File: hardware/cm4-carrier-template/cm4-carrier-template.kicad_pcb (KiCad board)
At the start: 4 copper layers, 90 x 40 mm, 41 parts, among them J1 USB_C_Receptacle_USB2.0, J2 Micro_SD_Card, J3 Abracon_ARJM11-502, Q1 DMP2066LSN, SW1 BOOT, SW2 GLOBAL_EN, U5 Compute_Module_4_Functional, U6 TPD2EUSB30

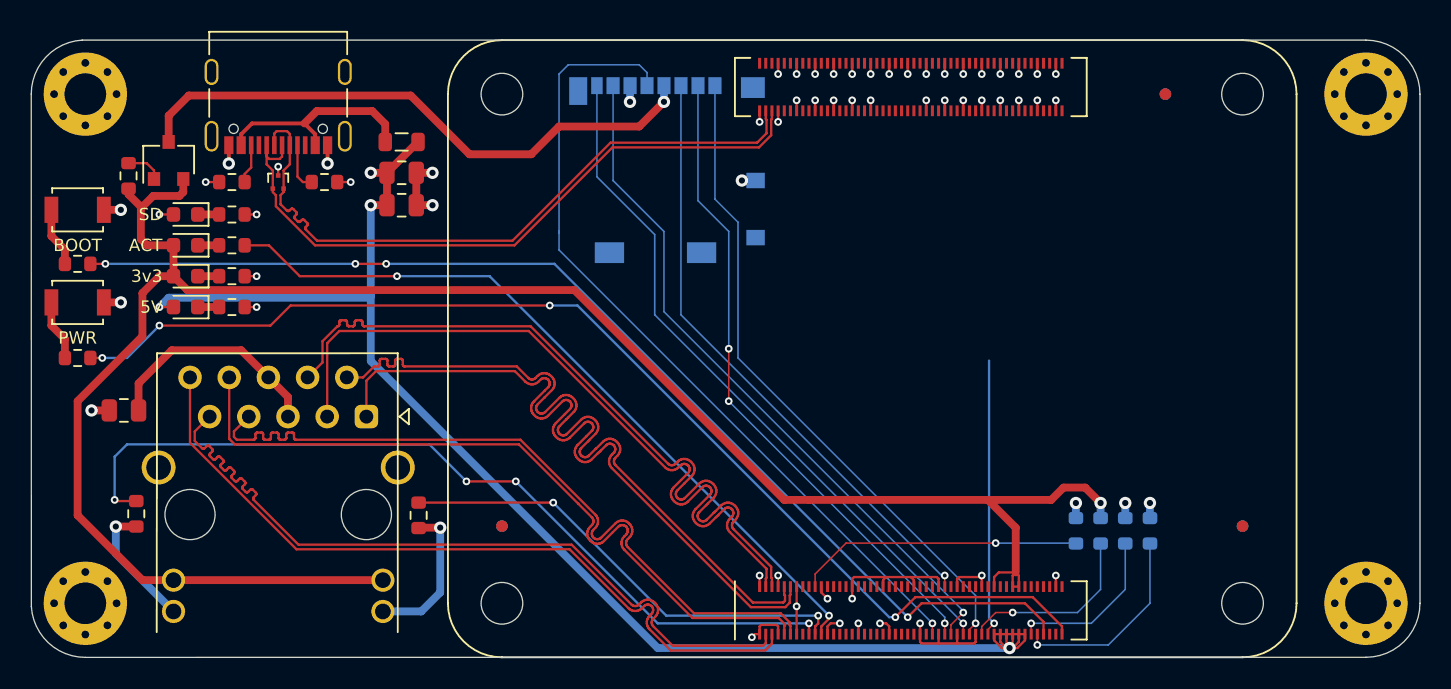
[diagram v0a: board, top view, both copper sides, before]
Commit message: Finished layout for 40mmx90mm base carrier.
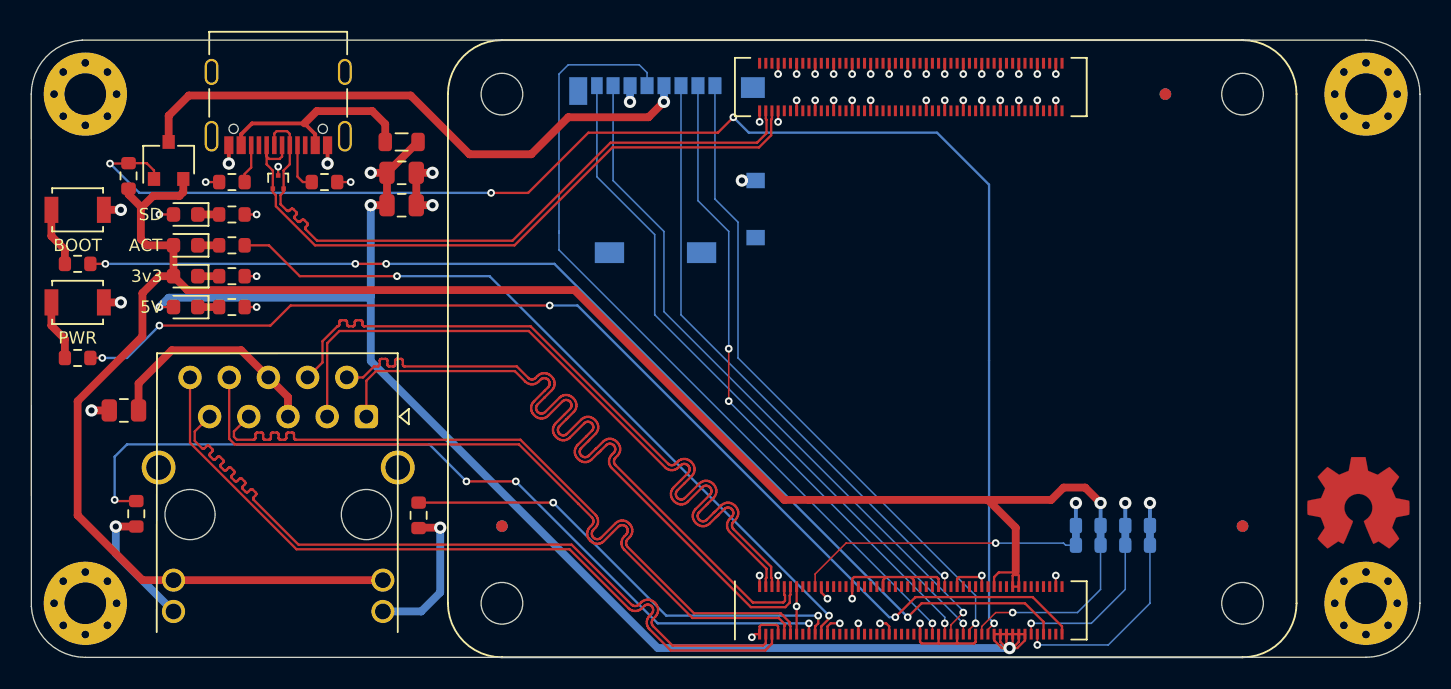
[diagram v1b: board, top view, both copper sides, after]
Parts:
- removed R13, R14, R15: 0R, Resistor_SMD:R_0603_1608Metric
- removed R5: DNP, Resistor_SMD:R_0603_1608Metric
- added JP1: eMMC, jkiv-library:J_Small_NC, B.Cu at (149.3, 126.1)
- added JP2: ~WL_nDisable, jkiv-library:J_Small_NC, B.Cu at (150.9, 126.1)
- added JP3: ~BT_nDisable, jkiv-library:J_Small_NC, B.Cu at (152.5, 126.1)
- added JP4: EEPROM_nWP, jkiv-library:J_Small_NC, B.Cu at (147.7, 126.1)
- added LOGO1: Logo_Open_Hardware_Small, Symbol:OSHW-Symbol_6.7x6mm_Copper, F.Cu at (166.0, 124.0)
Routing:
- net /SD_PWR_ON: track 20.4 -> 94.6 mm, vias 1 -> 4
- net GND: track 71.8 -> 73.3 mm
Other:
- board text added: "eMMC"
- board text removed: "~SD"

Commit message: Small adjustment to signal paths to make space on backside.
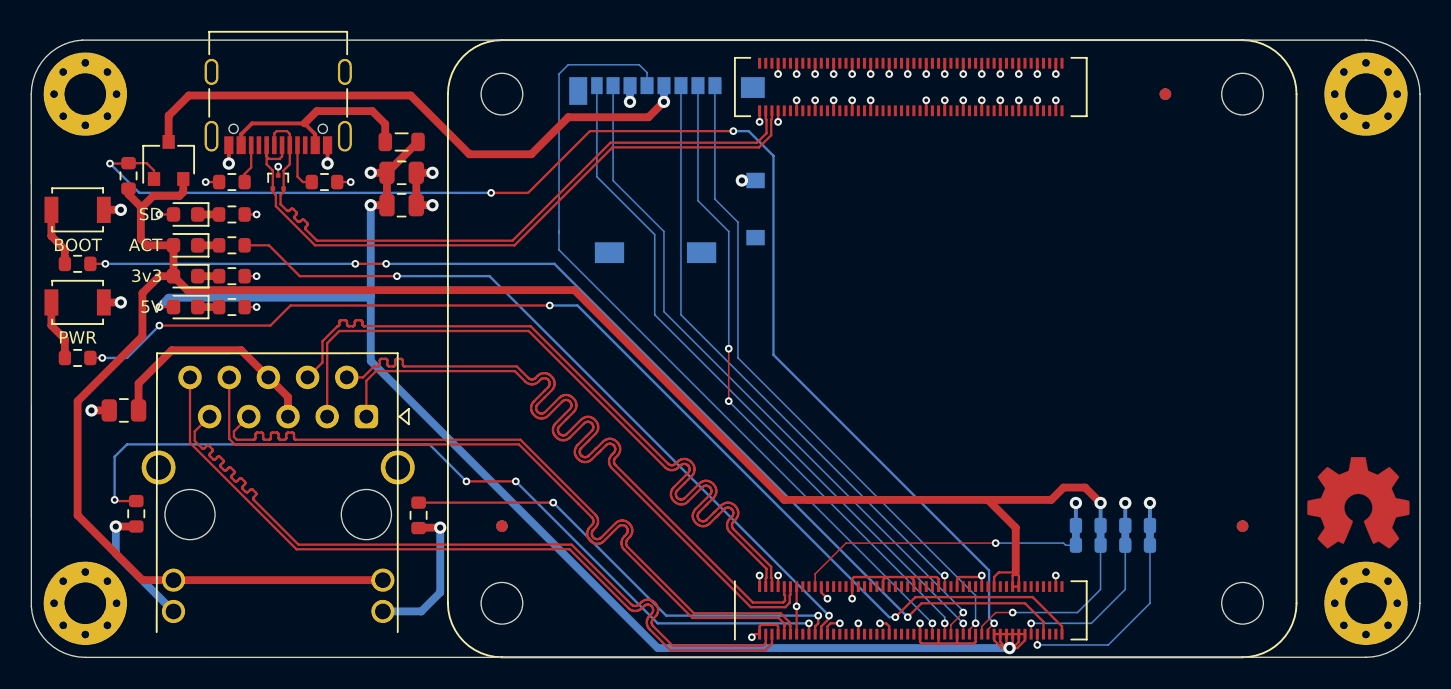
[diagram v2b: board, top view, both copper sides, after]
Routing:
- net /SD_PWR_ON: track 94.6 -> 86.8 mm

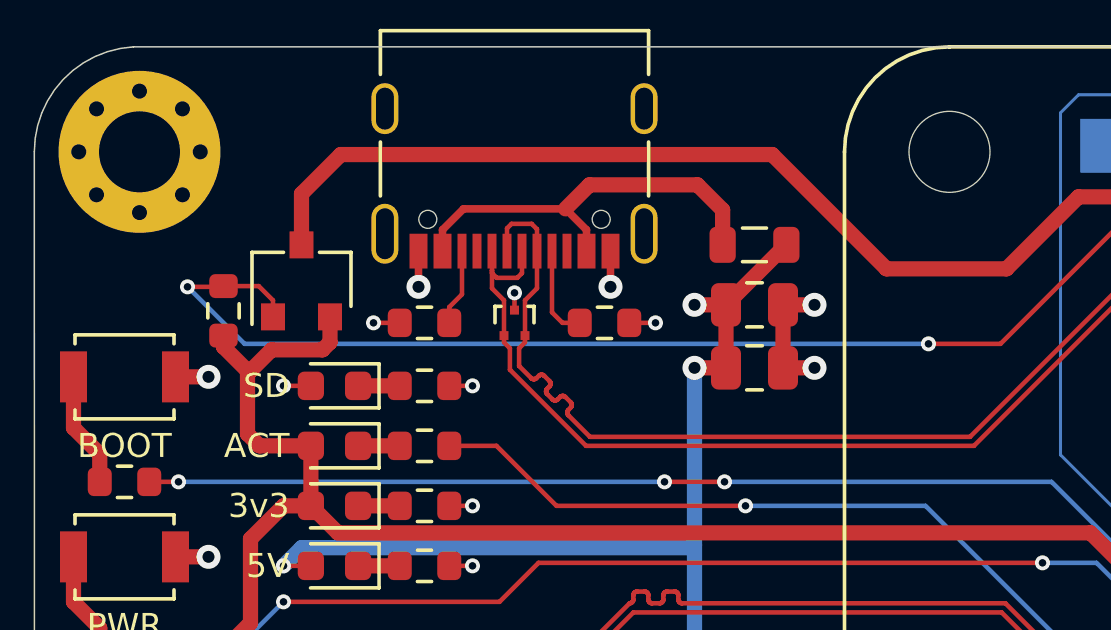
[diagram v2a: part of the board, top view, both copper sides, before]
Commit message: Fixed disconnected 'SD enabled' LED.
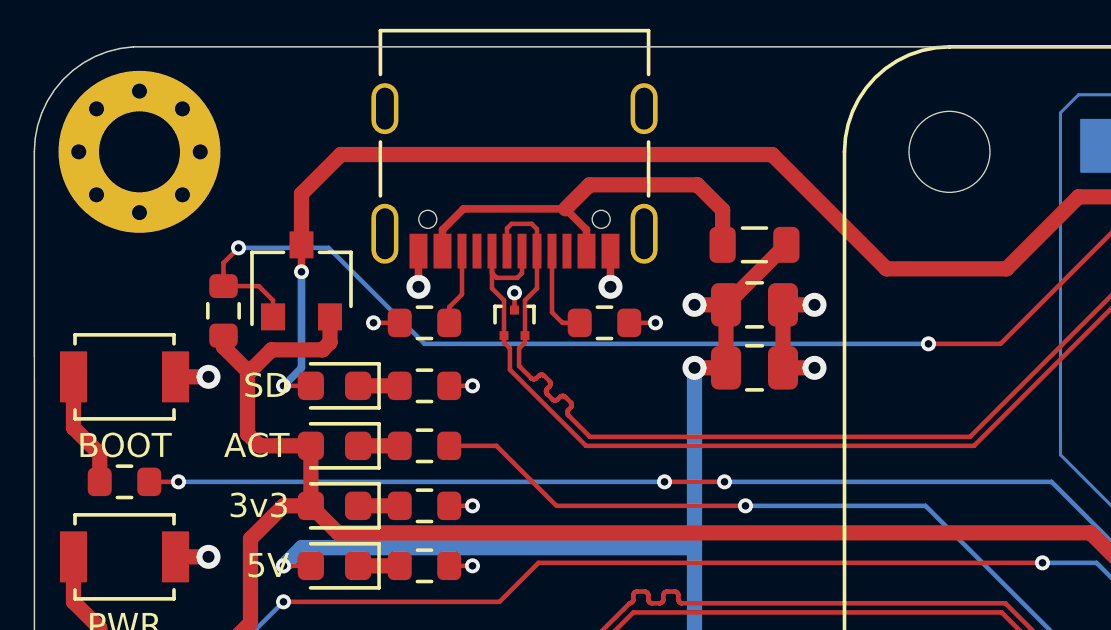
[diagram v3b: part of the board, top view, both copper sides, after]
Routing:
- net /SD_PWR: track 39.3 -> 44.2 mm, vias 2 -> 3
- net /SD_PWR_ON: track 86.8 -> 85.9 mm

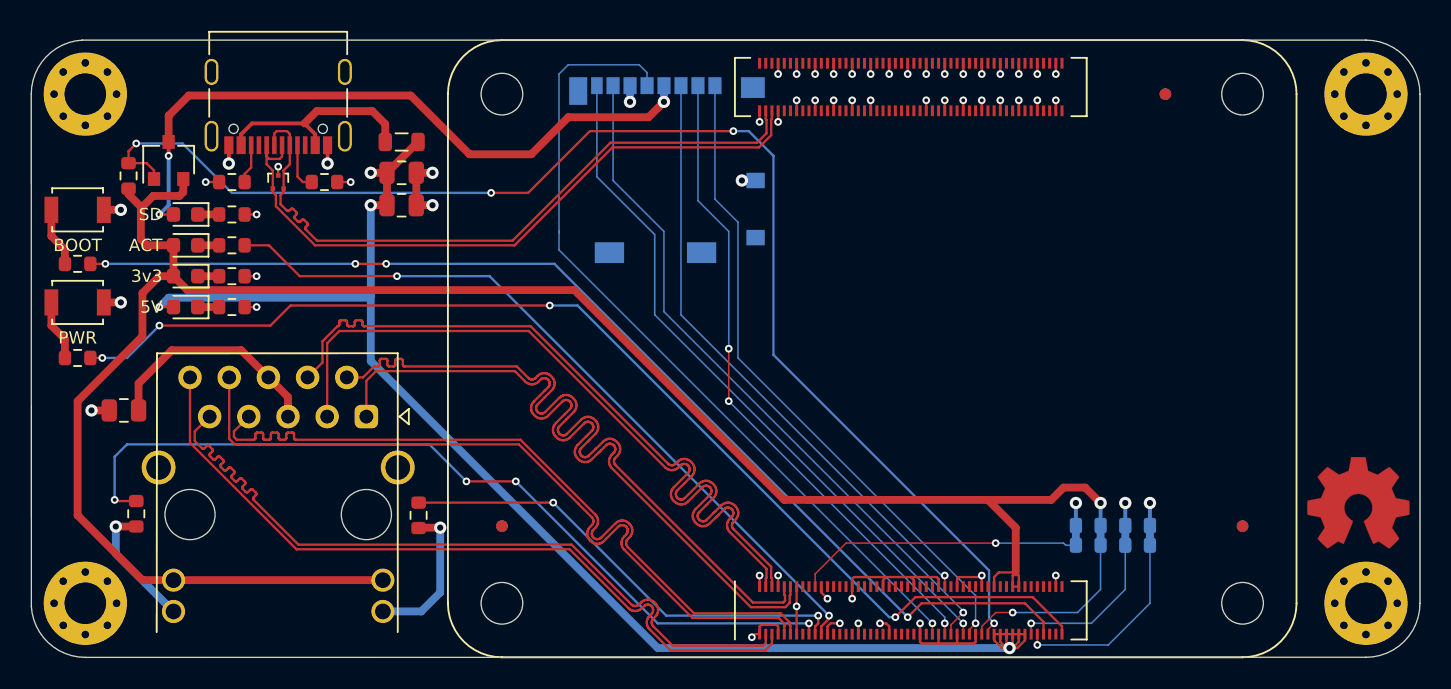
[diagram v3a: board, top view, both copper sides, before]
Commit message: Updated USB connector to what is available. Generated gerbers, HTMLBOM.
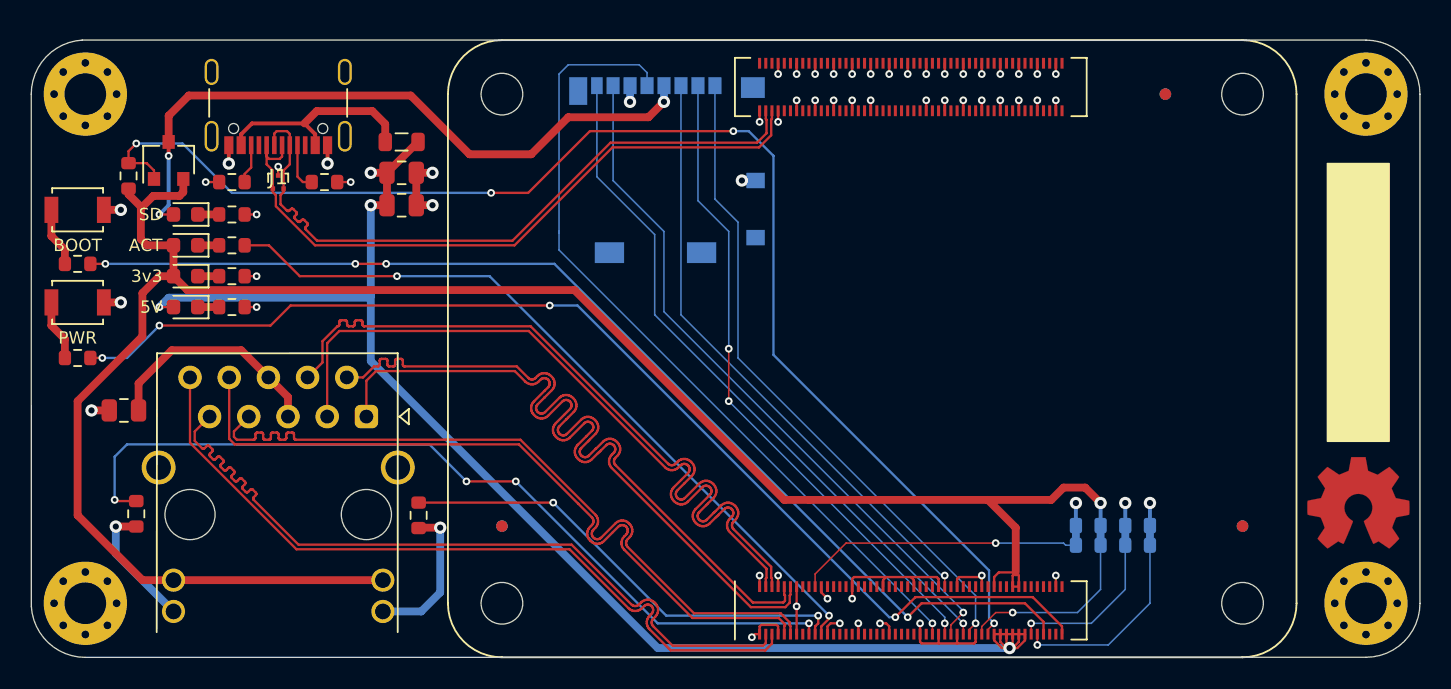
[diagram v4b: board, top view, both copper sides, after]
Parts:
- J1: footprint Connector_USB:USB_C_Receptacle_Palconn_UTC16-G -> jkiv-library:USB_C_Receptacle_GCT-USB4105
